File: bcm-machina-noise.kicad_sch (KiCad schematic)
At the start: 61 parts, among them J1 USB_A, J2 AVR-ISP-6, J3 AudioJack2_SwitchT, J5 AudioJack2_SwitchT, Q1 2N5457, Q2 2N5457, SW1 SW_Push, SW2 SW_Push, U1 4069, U2 MCP602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

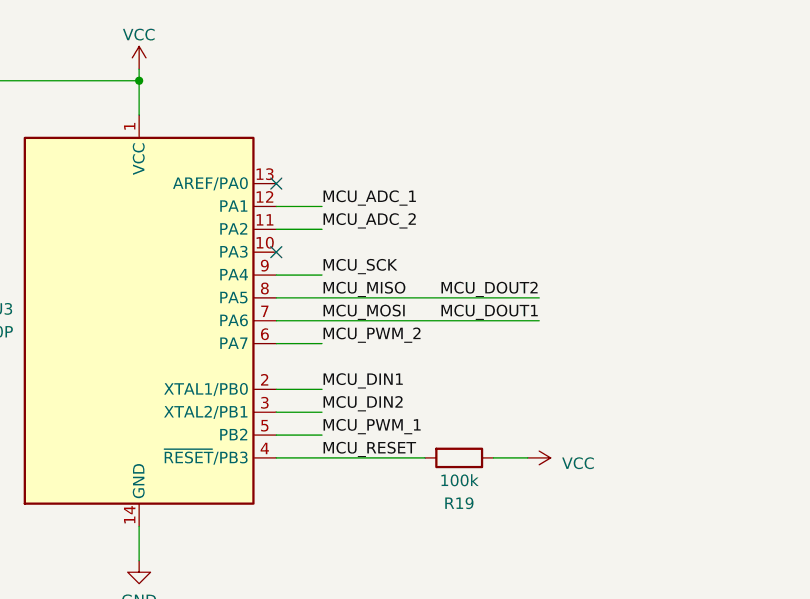
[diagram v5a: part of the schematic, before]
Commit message: USB traces fixed
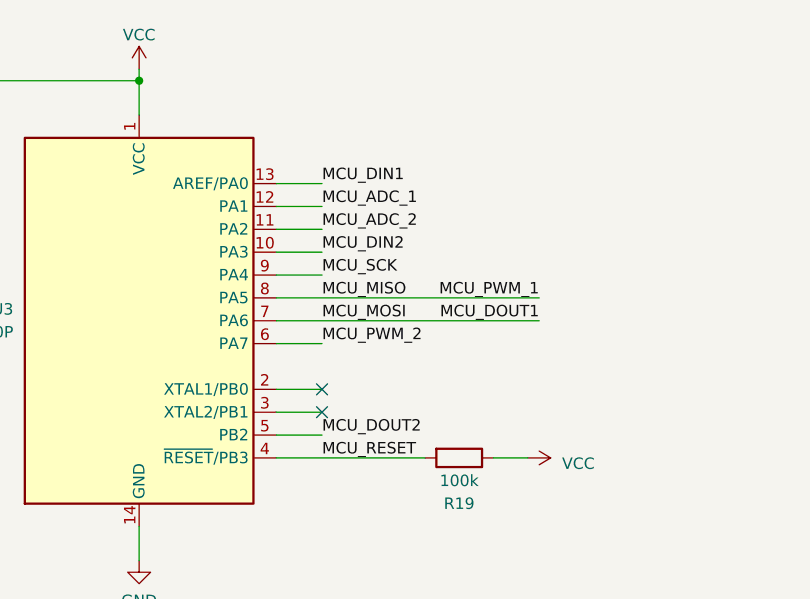
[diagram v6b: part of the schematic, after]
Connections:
- net MCU_DIN1: now also U3.13 (AREF/PA0); no longer U3.2 (XTAL1/PB0)
- net MCU_DIN2: now also U3.10 (PA3); no longer U3.3 (XTAL2/PB1)
- net MCU_DOUT2: now also U3.5 (PB2); no longer J2.1 (MISO), U3.8 (PA5)
- net MCU_PWM_1 renamed MCU_MISO
- net MCU_MISO: now also J2.1 (MISO), U3.8 (PA5); no longer U3.5 (PB2)
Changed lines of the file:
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@@
   (no_connect (at 223.52 105.41))
   (no_connect (at 354.33 48.26))
-  (no_connect (at 104.14 88.9))
   (no_connect (at 45.72 49.53))
   (no_connect (at 213.36 167.64))
@@
   (no_connect (at 354.33 35.56))
   (no_connect (at 45.72 46.99))
-  (no_connect (at 104.14 96.52))
+  (no_connect (at 109.22 114.3))
+  (no_connect (at 109.22 111.76))
   (wire (pts (xy 281.94 83.82) (xy 281.94 69.85))
     (stroke (width 0) (type default))
@@
     (stroke (width 0) (type default))
   )
+  (wire (pts (xy 104.14 88.9) (xy 109.22 88.9))
+    (stroke (width 0) (type default))
+  )
   (wire (pts (xy 335.28 91.44) (xy 332.74 91.44))
     (stroke (width 0) (type default))
@@
     (stroke (width 0) (type default))
   )
+  (wire (pts (xy 104.14 96.52) (xy 109.22 96.52))
+    (stroke (width 0) (type default))
+  )
   (wire (pts (xy 285.75 93.98) (xy 298.45 93.98))
     (stroke (width 0) (type default))
@@
     (effects (font (size 1.27 1.27)) (justify left bottom))
   )
-  (label "MCU_DIN1" (at 109.22 111.76 0) (fields_autoplaced)
-    (effects (font (size 1.27 1.27)) (justify left bottom))
-  )
-  (label "MCU_DOUT2" (at 133.35 101.6 180) (fields_autoplaced)
+  (label "MCU_DIN1" (at 109.22 88.9 0) (fields_autoplaced)
+    (effects (font (size 1.27 1.27)) (justify left bottom))
+  )
+  (label "MCU_DOUT2" (at 109.22 116.84 0) (fields_autoplaced)
+    (effects (font (size 1.27 1.27)) (justify left bottom))
+  )
+  (label "MCU_PWM_1" (at 133.35 101.6 180) (fields_autoplaced)
     (effects (font (size 1.27 1.27)) (justify right bottom))
   )
-  (label "MCU_PWM_1" (at 109.22 116.84 0) (fields_autoplaced)
-    (effects (font (size 1.27 1.27)) (justify left bottom))
-  )
   (label "MCU_ADC_2" (at 109.22 93.98 0) (fields_autoplaced)
     (effects (font (size 1.27 1.27)) (justify left bottom))
@@
     (effects (font (size 1.27 1.27)) (justify left bottom))
   )
-  (label "MCU_DIN2" (at 109.22 114.3 0) (fields_autoplaced)
-    (effects (font (size 1.27 1.27)) (justify left bottom))
-  )
+  (label "MCU_DIN2" (at 109.22 96.52 0) (fields_autoplaced)
+    (effects (font (size 1.27 1.27)) (justify left bottom))
+  )

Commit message: Finalising traces and ground plane, all errors removed
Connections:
- net GND: no longer J1.4 (GND)
- no-connect marks 12 -> 13
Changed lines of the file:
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@@
   (junction (at 255.27 49.53) (diameter 0) (color 0 0 0 0)
-  )
-  (junction (at 38.1 58.42) (diameter 0) (color 0 0 0 0)
   )
   (junction (at 227.33 76.2) (diameter 0) (color 0 0 0 0)
@@
   (no_connect (at 223.52 105.41))
   (no_connect (at 354.33 48.26))
+  (no_connect (at 38.1 57.15))
   (no_connect (at 45.72 49.53))
   (no_connect (at 213.36 167.64))
@@
     (stroke (width 0) (type default))
   )
-  (wire (pts (xy 50.8 58.42) (xy 50.8 57.15))
+  (wire (pts (xy 41.91 58.42) (xy 41.91 59.69))
     (stroke (width 0) (type default))
   )
@@
     (stroke (width 0) (type default))
   )
-  (wire (pts (xy 38.1 58.42) (xy 38.1 57.15))
-    (stroke (width 0) (type default))
-  )
   (wire (pts (xy 247.65 76.2) (xy 247.65 64.77))
     (stroke (width 0) (type default))
@@
     (stroke (width 0) (type default))
   )
-  (wire (pts (xy 38.1 58.42) (xy 50.8 58.42))
-    (stroke (width 0) (type default))
-  )
   (wire (pts (xy 243.84 220.98) (xy 243.84 226.06))
     (stroke (width 0) (type default))
@@
     (stroke (width 0) (type default))
   )
-  (wire (pts (xy 38.1 58.42) (xy 35.56 58.42))
+  (wire (pts (xy 35.56 58.42) (xy 41.91 58.42))
     (stroke (width 0) (type default))
   )
@@
     )
   )
-  (symbol (lib_id "power:PWR_FLAG") (at 50.8 57.15 0) (unit 1)
-    (in_bom yes) (on_board yes) (dnp no) (fields_autoplaced)
-    (property "Reference" "#FLG02" (at 50.8 55.245 0)
-      (effects (font (size 1.27 1.27)) hide)
-    )
-    (property "Value" "PWR_FLAG" (at 50.8 52.07 0)
-      (effects (font (size 1.27 1.27)))
-    )
-    (property "Footprint" "" (at 50.8 57.15 0)
-      (effects (font (size 1.27 1.27)) hide)
-    )
-    (property "Datasheet" "~" (at 50.8 57.15 0)
-      (effects (font (size 1.27 1.27)) hide)
-    )
+  (symbol (lib_id "power:PWR_FLAG") (at 41.91 59.69 180) (unit 1)
+    (in_bom yes) (on_board yes) (dnp no) (fields_autoplaced)
+    (property "Reference" "#FLG02" (at 41.91 61.595 0)
+      (effects (font (size 1.27 1.27)) hide)
+    )
+    (property "Value" "PWR_FLAG" (at 44.45 60.96 0)
+      (effects (font (size 1.27 1.27)) (justify right))
+    )
+    (property "Footprint" "" (at 41.91 59.69 0)
+      (effects (font (size 1.27 1.27)) hide)
+    )
+    (property "Datasheet" "~" (at 41.91 59.69 0)
+      (effects (font (size 1.27 1.27)) hide)
+    )

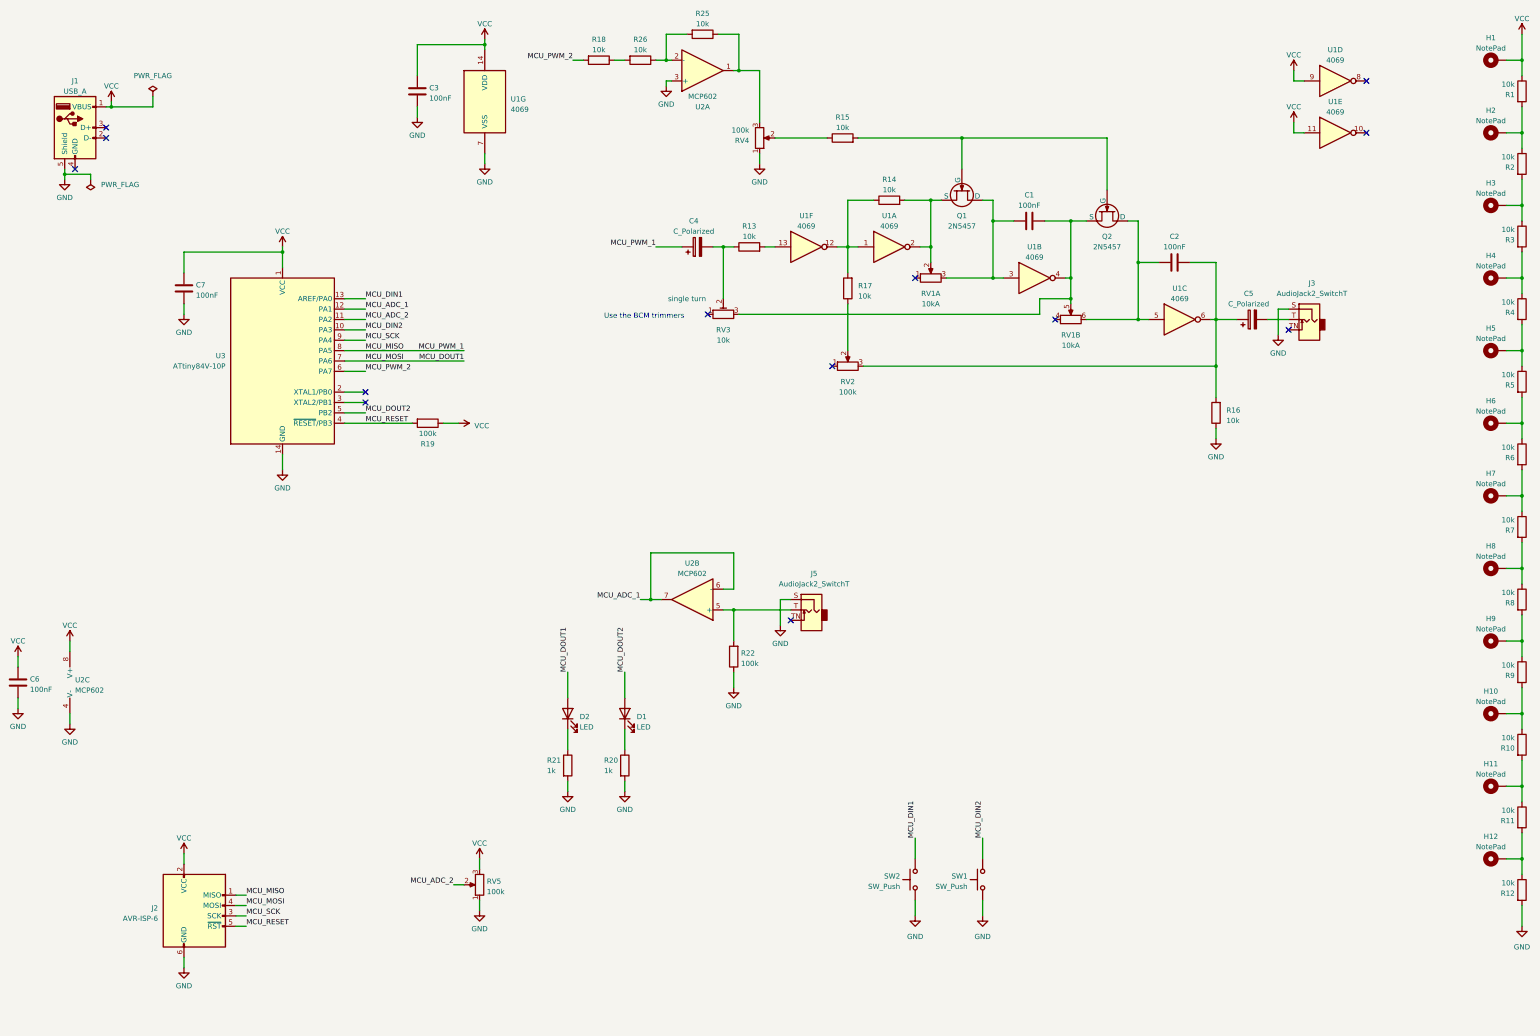
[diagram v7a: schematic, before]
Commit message: Fixing circuit for LFO output
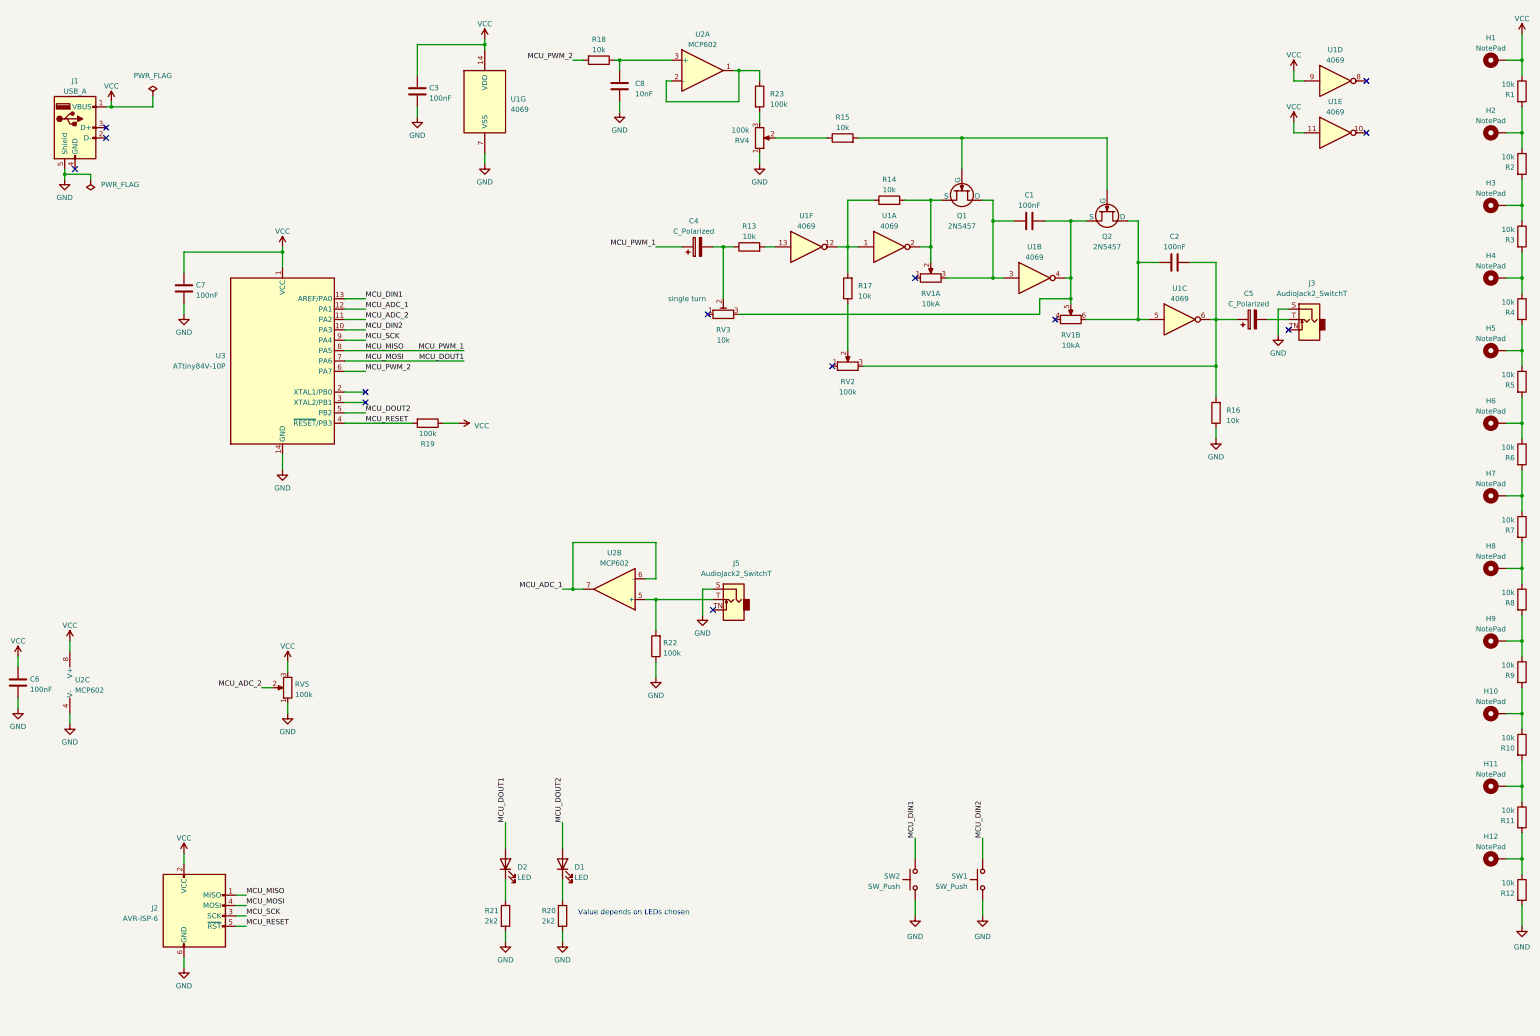
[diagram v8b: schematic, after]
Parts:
- removed R25, R26: 10k, Resistor_THT:R_Axial_DIN0207_L6.3mm_D2.5mm_P10.16mm_Horizontal, symbol Device:R
- added C8: 10nF, Capacitor_THT:C_Rect_L7.0mm_W3.5mm_P5.00mm, symbol Device:C
- added R23: 100k, Resistor_THT:R_Axial_DIN0207_L6.3mm_D2.5mm_P10.16mm_Horizontal, symbol Device:R
- C1, C2: Spec ceramic C0G -> film
- H1, H10, H11, H12, H2, H3, H4, H5, H6, H7, H8, H9: now left out of the parts list
- R20, R21: value 1k -> 2k2
- SW2: Part (none) -> Omron B3F-1070 Extended
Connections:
- net GND: now also C8.1; no longer U2.3 (+)
- net at U2.1: now also U2.2 (-), R23.1; no longer RV4.3
- net at R18.1: now also U2.3 (+), C8.2
- new net: R23.2, RV4.3
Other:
- note added: "Value depends on LEDs chosen"
- note removed: "Use the BCM trimmers"
- moved on the sheet: D1, D2, J5, R20, R21, R22, RV5, U2B
